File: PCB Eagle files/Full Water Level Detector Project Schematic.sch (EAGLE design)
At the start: 23 parts, among them IC1 74AHCT125

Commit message: PCB Layout WIP archive
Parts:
- added ELEC-LEFT, ELEC-RIGHT: (no value), con-lstb:MA06-1
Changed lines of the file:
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@@
 <part name="GND13" library="SparkFun-Aesthetics" deviceset="GND" device=""/>
 <part name="GND10" library="SparkFun-Aesthetics" deviceset="GND" device=""/>
+<part name="ELEC-LEFT" library="con-lstb" deviceset="MA06-1" device=""/>
+<part name="ELEC-RIGHT" library="con-lstb" deviceset="MA06-1" device=""/>
 </parts>
 <sheets>
@@
 <instance part="GND13" gate="1" x="45.72" y="78.74"/>
 <instance part="GND10" gate="1" x="60.96" y="88.9"/>
+<instance part="ELEC-LEFT" gate="1" x="-20.32" y="124.46"/>
+<instance part="ELEC-RIGHT" gate="1" x="2.54" y="124.46"/>
 </instances>
 <busses>

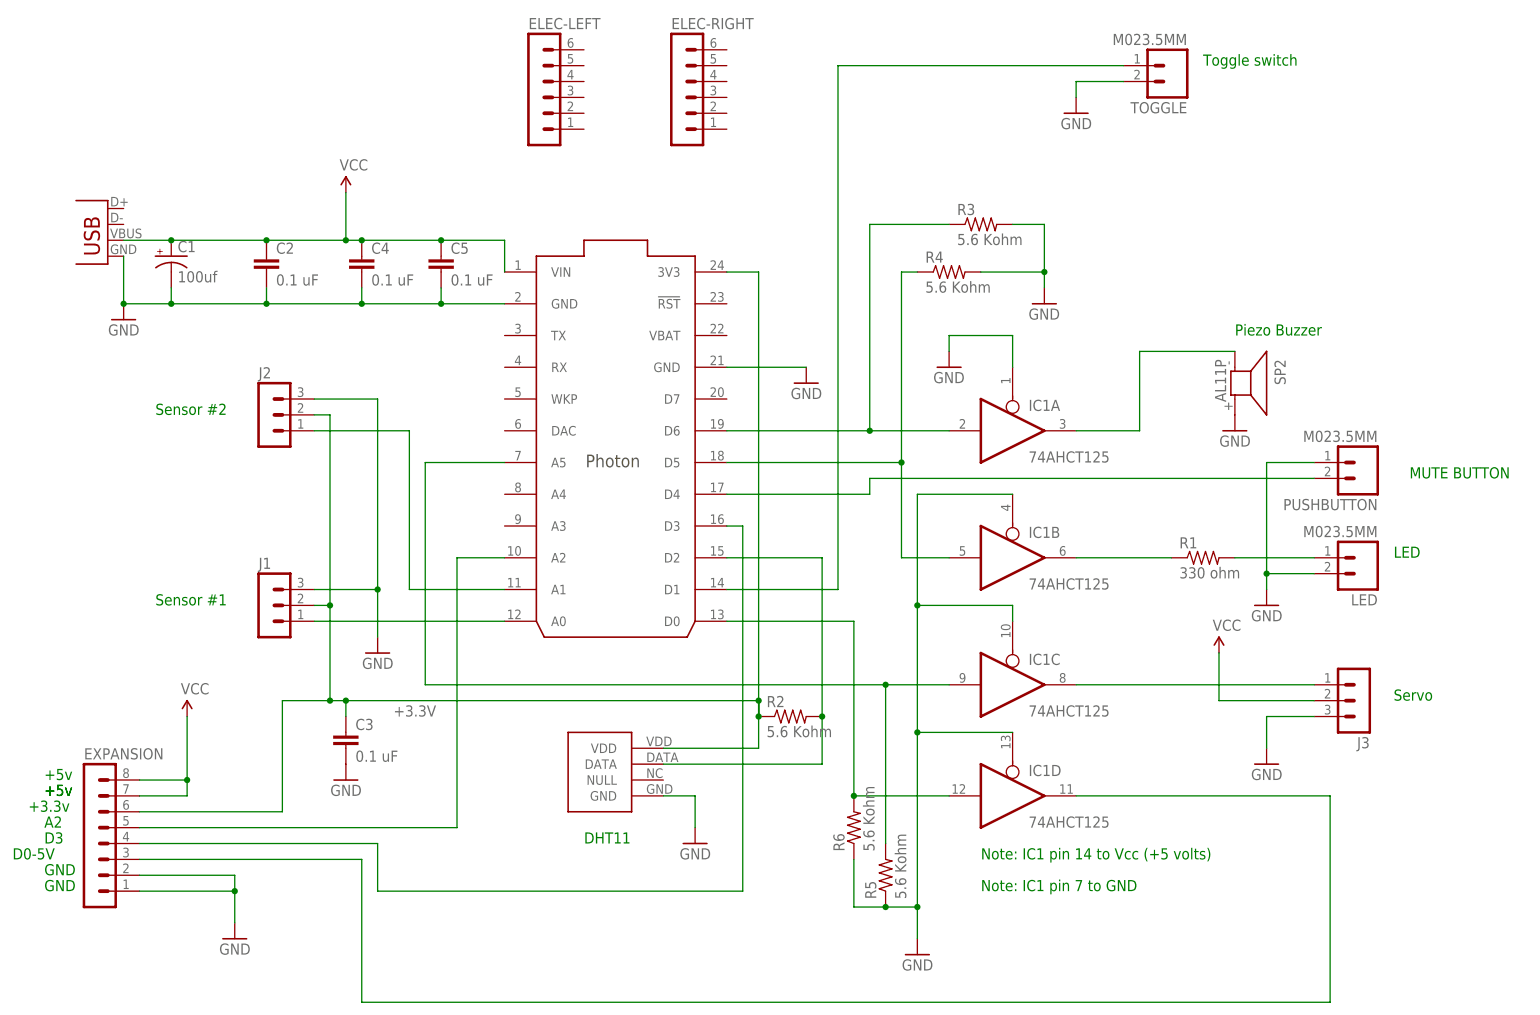
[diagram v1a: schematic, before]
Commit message: Updated schematic
Changed mini screw terminals to pin headers.  Completed board placement
and routing, but still need the ground pour.
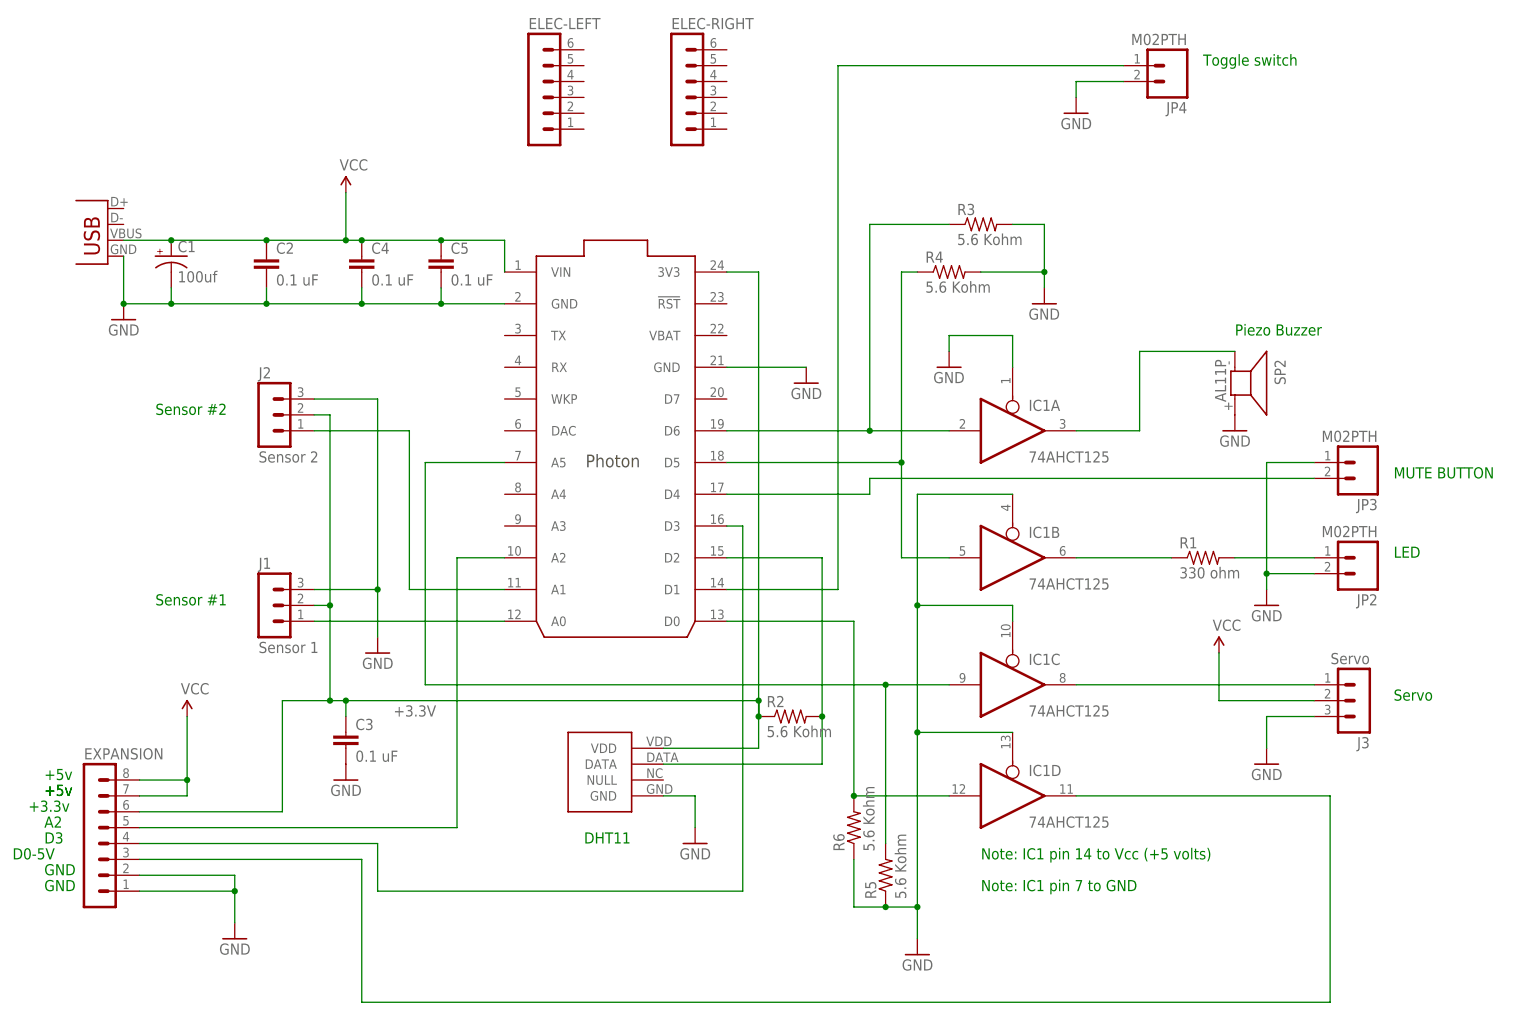
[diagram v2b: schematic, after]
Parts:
- removed LED, PUSHBUTTON, TOGGLE: M023.5MM, SparkFun-Connectors:M023.5MM
- added JP2, JP3, JP4: M02PTH, SparkFun-Connectors:M02PTH
- J1: value (none) -> Sensor 1
- J2: value (none) -> Sensor 2
- J3: value (none) -> Servo
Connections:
- net GND: now also JP2.2, JP3.1, JP4.2; no longer LED.2, PUSHBUTTON.1, TOGGLE.2
- net N$10: now also JP2.1; no longer LED.1
- net N$11: now also JP3.2; no longer PUSHBUTTON.2
- net N$22: now also JP4.1; no longer TOGGLE.1
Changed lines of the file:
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@@
 <parts>
 <part name="U$1" library="Spark" deviceset="PHOTON_SMD" device=""/>
-<part name="J1" library="con-lstb" deviceset="MA03-1" device=""/>
-<part name="J2" library="con-lstb" deviceset="MA03-1" device=""/>
+<part name="J1" library="con-lstb" deviceset="MA03-1" device="" value="Sensor 1"/>
+<part name="J2" library="con-lstb" deviceset="MA03-1" device="" value="Sensor 2"/>
 <part name="GND1" library="SparkFun-Aesthetics" deviceset="GND" device=""/>
 <part name="JP1" library="SparkFun-Connectors" deviceset="USB" device="PTH" value="USB-B"/>
@@
 <part name="GND7" library="SparkFun-Aesthetics" deviceset="GND" device=""/>
 <part name="SUPPLY1" library="SparkFun-Aesthetics" deviceset="VCC" device=""/>
-<part name="J3" library="con-lstb" deviceset="MA03-1" device=""/>
+<part name="J3" library="con-lstb" deviceset="MA03-1" device="" value="Servo"/>
 <part name="SUPPLY2" library="SparkFun-Aesthetics" deviceset="VCC" device=""/>
 <part name="GND4" library="SparkFun-Aesthetics" deviceset="GND" device=""/>
@@
 <part name="C4" library="SparkFun-Passives" deviceset="CAP" device="PTH" value="0.1 uF"/>
 <part name="C5" library="SparkFun-Passives" deviceset="CAP" device="PTH" value="0.1 uF"/>
-<part name="TOGGLE" library="SparkFun-Connectors" deviceset="M02" device="3.5MM"/>
-<part name="PUSHBUTTON" library="SparkFun-Connectors" deviceset="M02" device="3.5MM"/>
-<part name="LED" library="SparkFun-Connectors" deviceset="M02" device="3.5MM"/>
 <part name="GND11" library="SparkFun-Aesthetics" deviceset="GND" device=""/>
 <part name="GND8" library="SparkFun-Aesthetics" deviceset="GND" device=""/>
@@
 <part name="ELEC-LEFT" library="con-lstb" deviceset="MA06-1" device=""/>
 <part name="ELEC-RIGHT" library="con-lstb" deviceset="MA06-1" device=""/>
+<part name="JP3" library="SparkFun-Connectors" deviceset="M02" device="PTH"/>
+<part name="JP2" library="SparkFun-Connectors" deviceset="M02" device="PTH"/>
+<part name="JP4" library="SparkFun-Connectors" deviceset="M02" device="PTH"/>
 </parts>
 <sheets>
@@
 <text x="50.8" y="-5.08" size="1.778" layer="91">Note: IC1 pin 7 to GND</text>
 <text x="86.36" y="127" size="1.778" layer="91">Toggle switch</text>
-<text x="119.38" y="60.96" size="1.778" layer="91">MUTE BUTTON</text>
+<text x="116.84" y="60.96" size="1.778" layer="91">MUTE BUTTON</text>
 <text x="116.84" y="48.26" size="1.778" layer="91">LED</text>
 <text x="-99.06" y="12.7" size="1.778" layer="91">+5v</text>
@@
 <instance part="C4" gate="G$1" x="-48.26" y="93.98"/>
 <instance part="C5" gate="G$1" x="-35.56" y="93.98"/>
-<instance part="TOGGLE" gate="G$1" x="81.28" y="127" rot="R180"/>
-<instance part="PUSHBUTTON" gate="G$1" x="111.76" y="63.5" rot="R180"/>
-<instance part="LED" gate="G$1" x="111.76" y="48.26" rot="R180"/>
 <instance part="GND11" gate="1" x="66.04" y="119.38" rot="MR0"/>
 <instance part="GND8" gate="1" x="96.52" y="40.64" rot="MR0"/>
@@
 <instance part="ELEC-LEFT" gate="1" x="-20.32" y="124.46"/>
 <instance part="ELEC-RIGHT" gate="1" x="2.54" y="124.46"/>
+<instance part="JP3" gate="G$1" x="111.76" y="63.5" rot="R180"/>
+<instance part="JP2" gate="G$1" x="111.76" y="48.26" rot="R180"/>
+<instance part="JP4" gate="G$1" x="81.28" y="127" rot="R180"/>
 </instances>
 <busses>
@@
 </segment>
 <segment>
-<pinref part="PUSHBUTTON" gate="G$1" pin="1"/>
 <pinref part="GND8" gate="1" pin="GND"/>
 <wire x1="104.14" y1="63.5" x2="96.52" y2="63.5" width="0.1524" layer="91"/>
 <wire x1="96.52" y1="63.5" x2="96.52" y2="45.72" width="0.1524" layer="91"/>
-<pinref part="LED" gate="G$1" pin="2"/>
 <wire x1="96.52" y1="45.72" x2="96.52" y2="43.18" width="0.1524" layer="91"/>
 <wire x1="104.14" y1="45.72" x2="96.52" y2="45.72" width="0.1524" layer="91"/>
 <junction x="96.52" y="45.72"/>
+<pinref part="JP3" gate="G$1" pin="1"/>
+<pinref part="JP2" gate="G$1" pin="2"/>
 </segment>
 <segment>
@@
 <pinref part="GND11" gate="1" pin="GND"/>
 <wire x1="66.04" y1="121.92" x2="66.04" y2="124.46" width="0.1524" layer="91"/>
-<pinref part="TOGGLE" gate="G$1" pin="2"/>
 <wire x1="66.04" y1="124.46" x2="73.66" y2="124.46" width="0.1524" layer="91"/>
+<pinref part="JP4" gate="G$1" pin="2"/>
 </segment>
 <segment>
@@
 <segment>
 <wire x1="33.02" y1="58.42" x2="33.02" y2="60.96" width="0.1524" layer="91"/>
-<pinref part="PUSHBUTTON" gate="G$1" pin="2"/>
 <wire x1="33.02" y1="60.96" x2="104.14" y2="60.96" width="0.1524" layer="91"/>
 <pinref part="U$1" gate="G$1" pin="D4"/>
 <wire x1="10.16" y1="58.42" x2="33.02" y2="58.42" width="0.1524" layer="91"/>
+<pinref part="JP3" gate="G$1" pin="2"/>
 </segment>
 </net>
@@
 <pinref part="U$1" gate="G$1" pin="D1"/>
 <wire x1="10.16" y1="43.18" x2="27.94" y2="43.18" width="0.1524" layer="91"/>
-<pinref part="TOGGLE" gate="G$1" pin="1"/>
 <wire x1="27.94" y1="127" x2="73.66" y2="127" width="0.1524" layer="91"/>
+<pinref part="JP4" gate="G$1" pin="1"/>
 </segment>
 </net>
@@
 <net name="N$10" class="0">
 <segment>
-<pinref part="LED" gate="G$1" pin="1"/>
 <pinref part="R1" gate="G$1" pin="2"/>
 <wire x1="104.14" y1="48.26" x2="91.44" y2="48.26" width="0.1524" layer="91"/>
-</segment>
-</net>
+<pinref part="JP2" gate="G$1" pin="1"/>
+</segment>
+</net>
